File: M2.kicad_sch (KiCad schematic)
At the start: 59 parts, among them J100 Bus_M.2_2199230-2, J6 Bus_M.2_1-2199230-6, Y1 Oscillator_32.768kHz_ECS_2520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

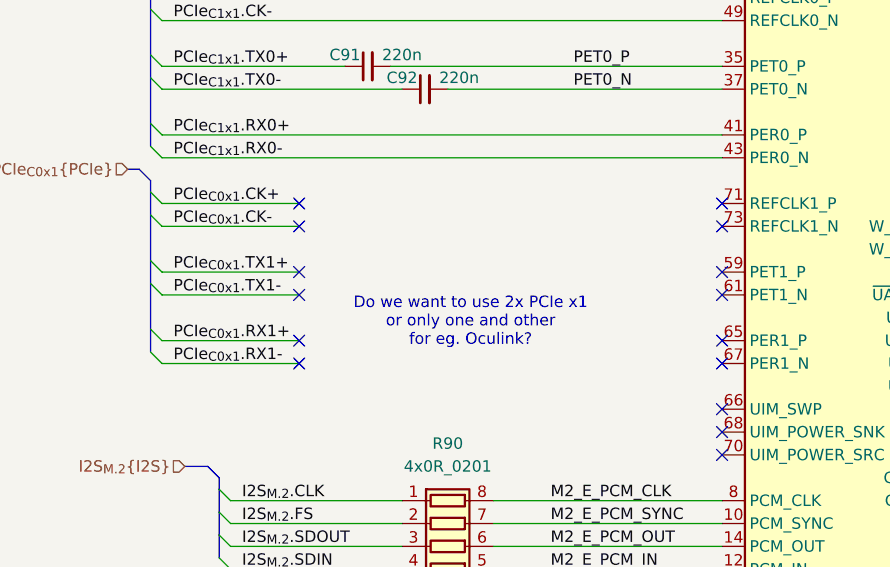
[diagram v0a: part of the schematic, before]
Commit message: [#81970] Route present on root GPIO pins on CSI and Peripherals sheets
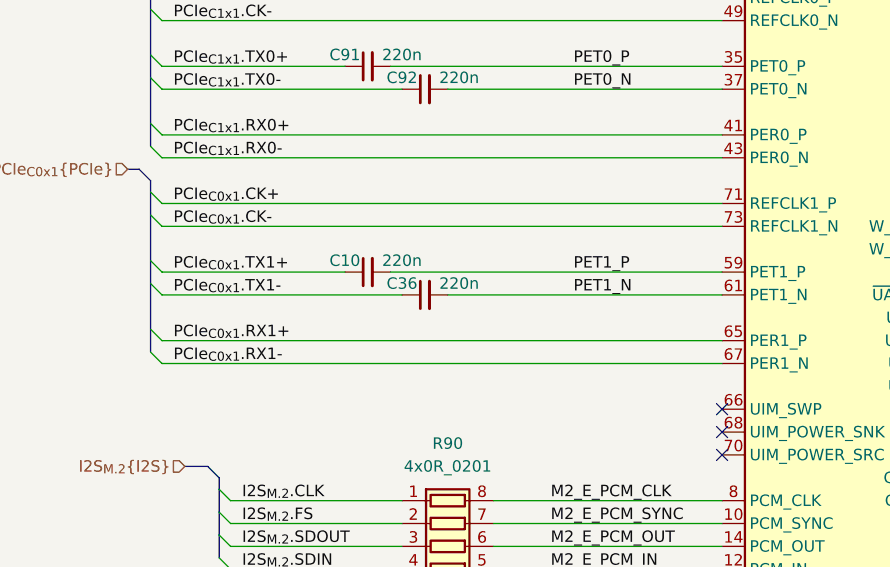
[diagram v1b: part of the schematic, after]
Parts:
- added C10, C36: C_220n_6V3_X7R_0402, antmicro-footprints:C_0402_1005Metric, symbol antmicroCapacitors0402:C_220n_6V3_X7R_0402
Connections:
- net PCIe_{C0x1}.CK+: now also J100.71 (REFCLK1_P)
- net PCIe_{C0x1}.CK-: now also J100.73 (REFCLK1_N)
- net PCIe_{C0x1}.RX1+: now also J100.65 (PER1_P)
- net PCIe_{C0x1}.RX1-: now also J100.67 (PER1_N)
- net PCIe_{C0x1}.TX1+: now also C10.1
- net PCIe_{C0x1}.TX1-: now also C36.1
- net PET1_N: now also J100.61 (PET1_N), C36.2
- net PET1_P: now also J100.59 (PET1_P), C10.2
- no-connect marks 29 -> 17
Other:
- note removed: "Do we want to use 2x PCIe x1 or only one and other for eg. Oculink?"

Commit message: [#82757] Rename project to jetson-agx-thor-baseboard
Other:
- title: Jetson Orin AGX Baseboard -> Jetson AGX Thor Baseboard
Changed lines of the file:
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@@
 	(paper "A3")
 	(title_block
-		(title "Jetson Orin AGX Baseboard")
+		(title "Jetson AGX Thor Baseboard")
 		(date "2025-08-11")
 		(rev "1.0.0")

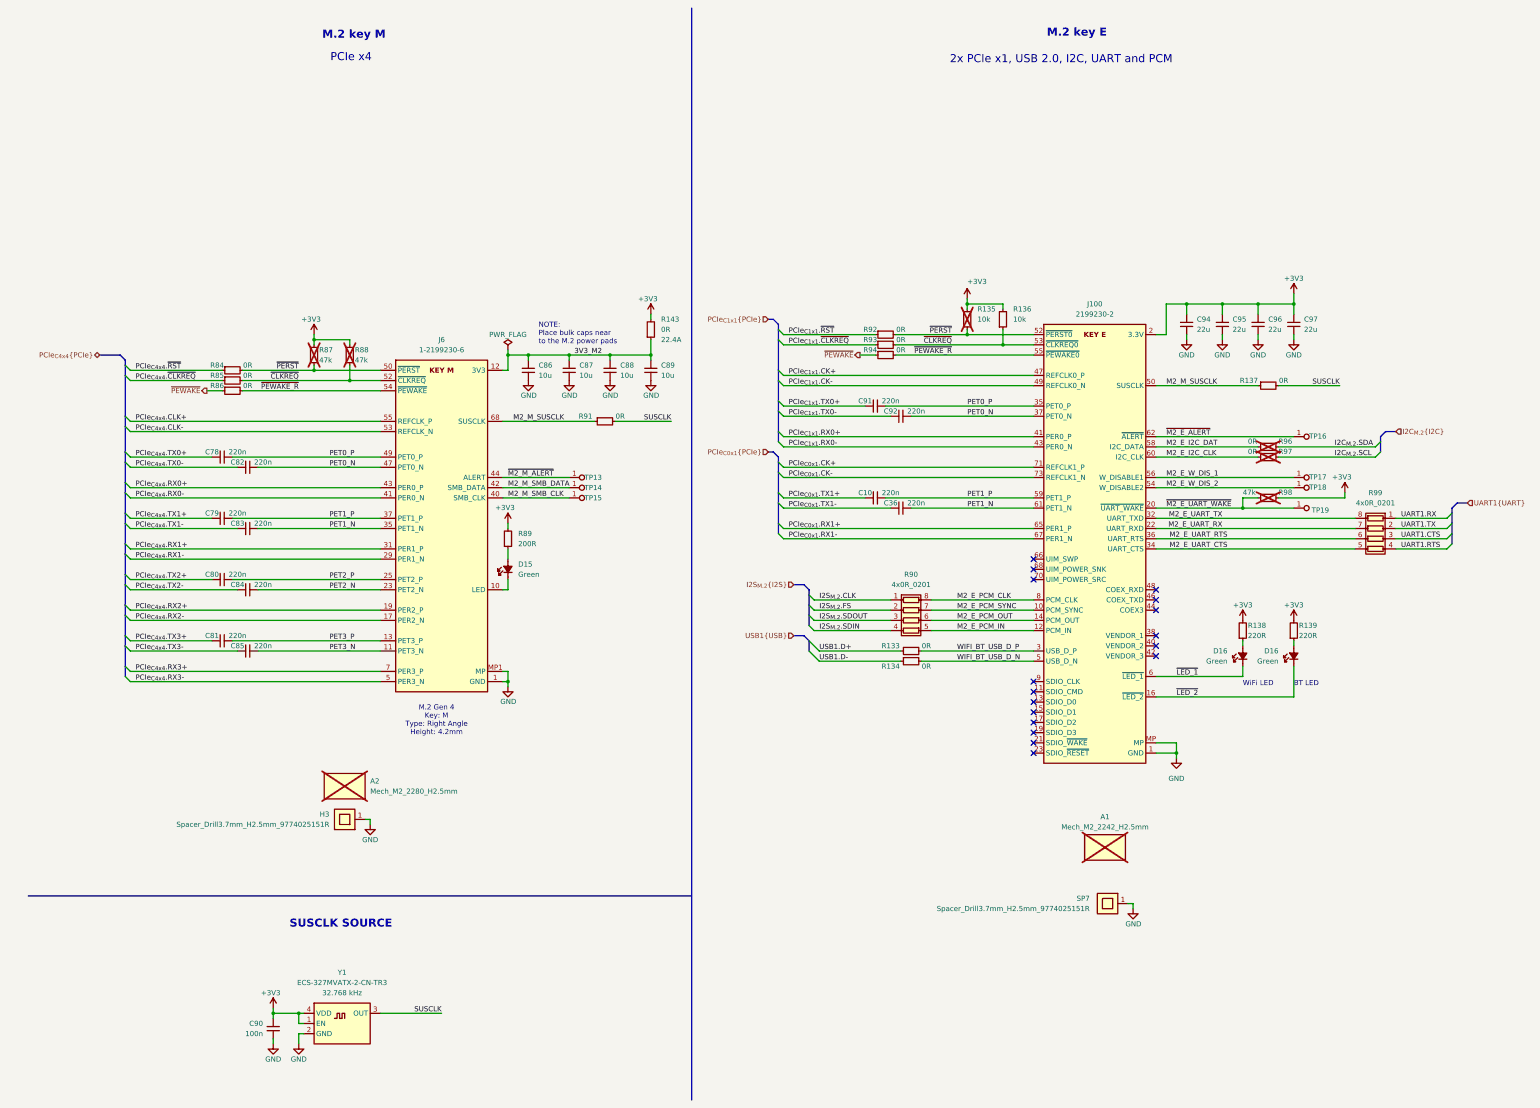
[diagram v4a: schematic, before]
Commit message: [#82757] Cleanup: reorganise page numbers and fix annotations
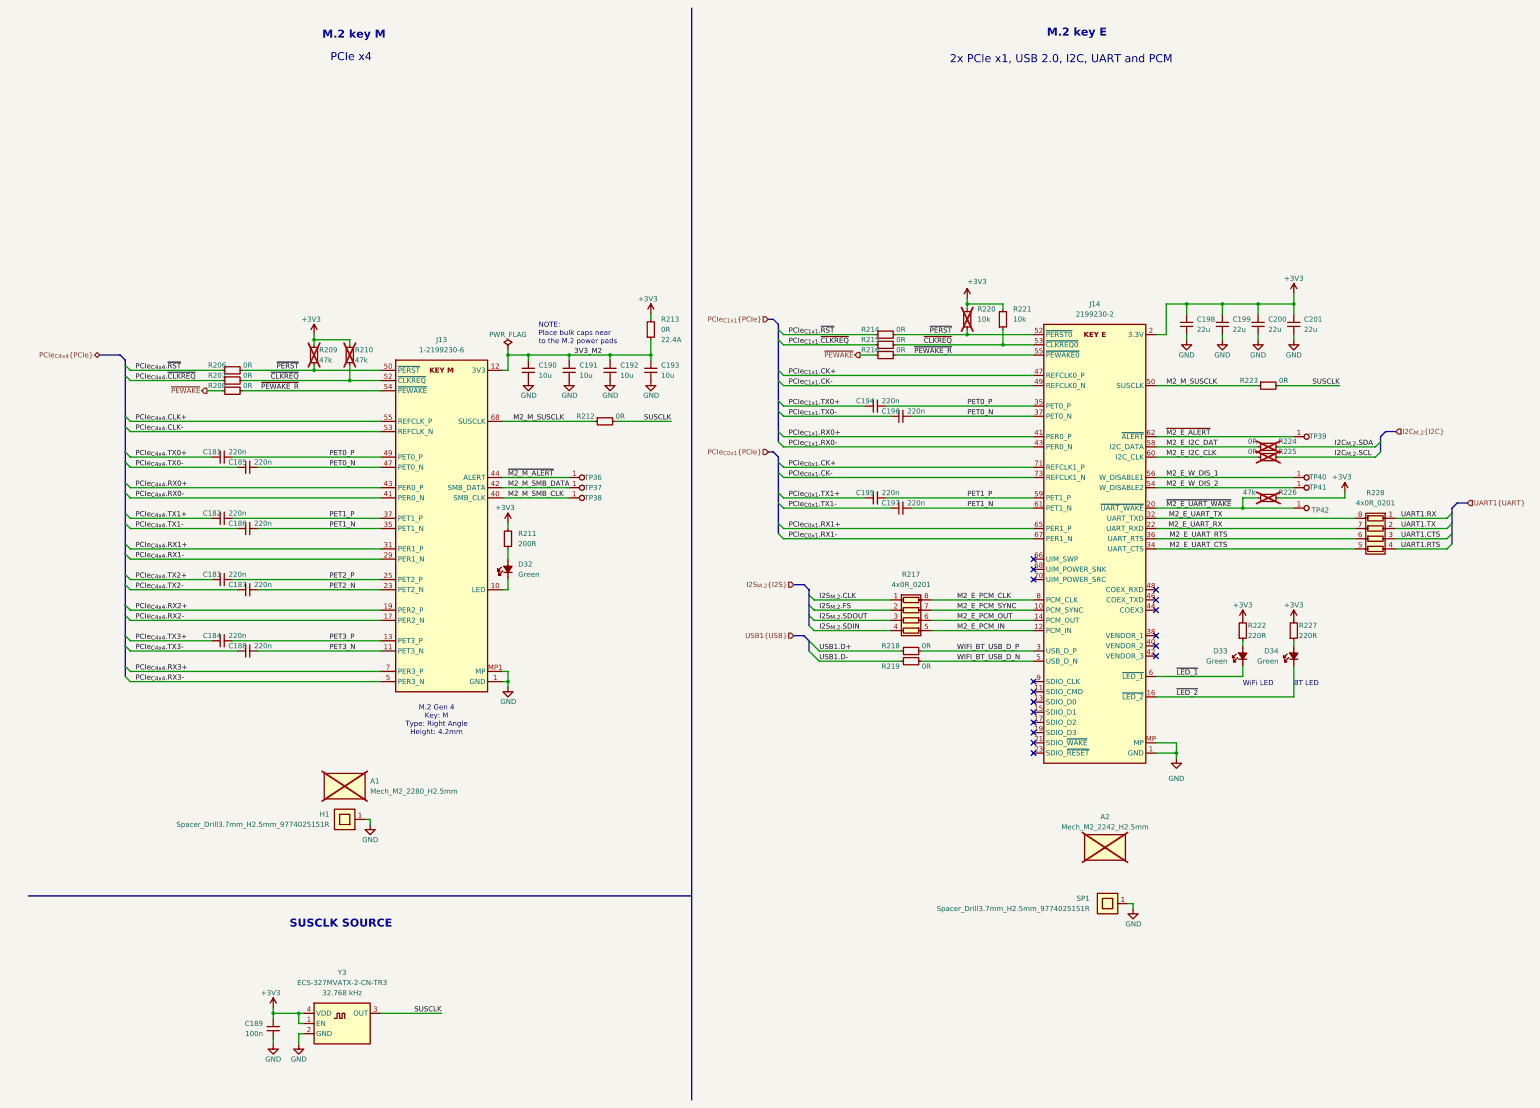
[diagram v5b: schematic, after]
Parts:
- renumbered A2 to A1, A1 to A2, C78 to C181, C79 to C182, C80 to C183, C81 to C184, C82 to C185, C83 to C186, C84 to C187, C85 to C188, C90 to C189, C86 to C190, C87 to C191, C88 to C192, C89 to C193, C91 to C194, C10 to C195, C92 to C196, C36 to C197, C94 to C198, C95 to C199, C96 to C200, C97 to C201, D15 to D32, D16 to D33, D16 to D34, H3 to H1, J6 to J13, J100 to J14, R84 to R206, R85 to R207, R86 to R208, R87 to R209, R88 to R210, R89 to R211, R91 to R212, R143 to R213, R92 to R214, R93 to R215, R94 to R216, R90 to R217, R133 to R218, R134 to R219, R135 to R220, R136 to R221, R138 to R222, R137 to R223, R96 to R224, R97 to R225, R98 to R226, R139 to R227, R99 to R228, SP7 to SP1, TP13 to TP36, TP14 to TP37, TP15 to TP38, TP16 to TP39, TP17 to TP40, TP18 to TP41, TP19 to TP42, Y1 to Y3
